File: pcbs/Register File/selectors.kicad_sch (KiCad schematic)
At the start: 33 parts, among them U1001 74HC138, U1002 74HC138, U1003 74HC138, U1004 74HC138, U1005 74HC540, U1006 74HC32, U1007 74HC14

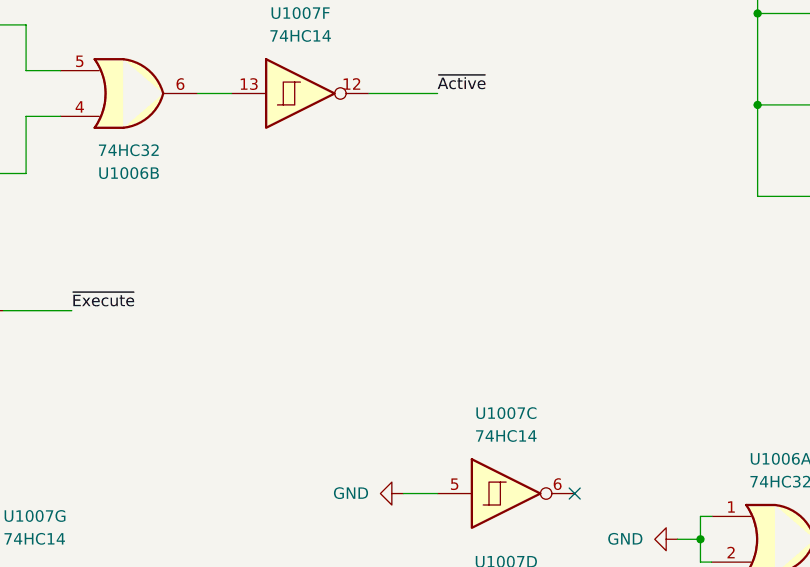
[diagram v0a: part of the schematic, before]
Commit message: Tester for the Register File (#59)
Create a test suite for the Register File. As noted in Issue #58 this has uncovered the fact that the register file is updating on 'Execute' when it should be updating on 'Commit' and the tests have to reflect this.
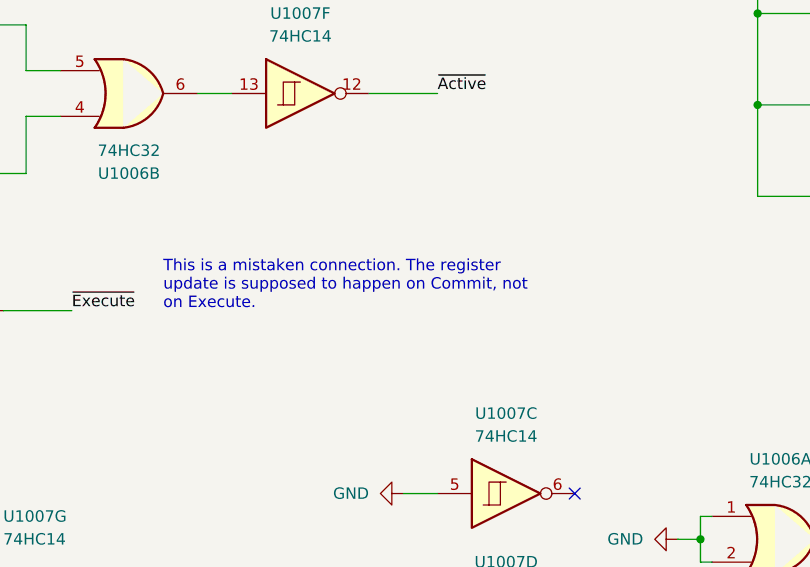
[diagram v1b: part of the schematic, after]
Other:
- note added: "This is a mistaken connection. The register update is supposed to happen on Commit, not on Execute."
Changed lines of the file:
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@@
     (stroke (width 0) (type default))
+  )
+  (text "This is a mistaken connection. The register\nupdate is supposed to happen on Commit, not\non Execute."
+    (at 71.12 151.13 0)
+    (effects (font (size 1.27 1.27)) (justify left bottom))
   )
   (label "R_{C}0" (at 31.75 63.5 0) (fields_autoplaced)
